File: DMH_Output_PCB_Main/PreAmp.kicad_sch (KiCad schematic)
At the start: 42 parts, among them J13 Conn_01x06, J28 Conn_01x06, J33 Conn_01x06, J35 Conn_01x04_PinHeader, J36 Conn_01x04_PinHeader, U16 NE5532, U17 NE5532, U18 NE5532, U19 NE5532

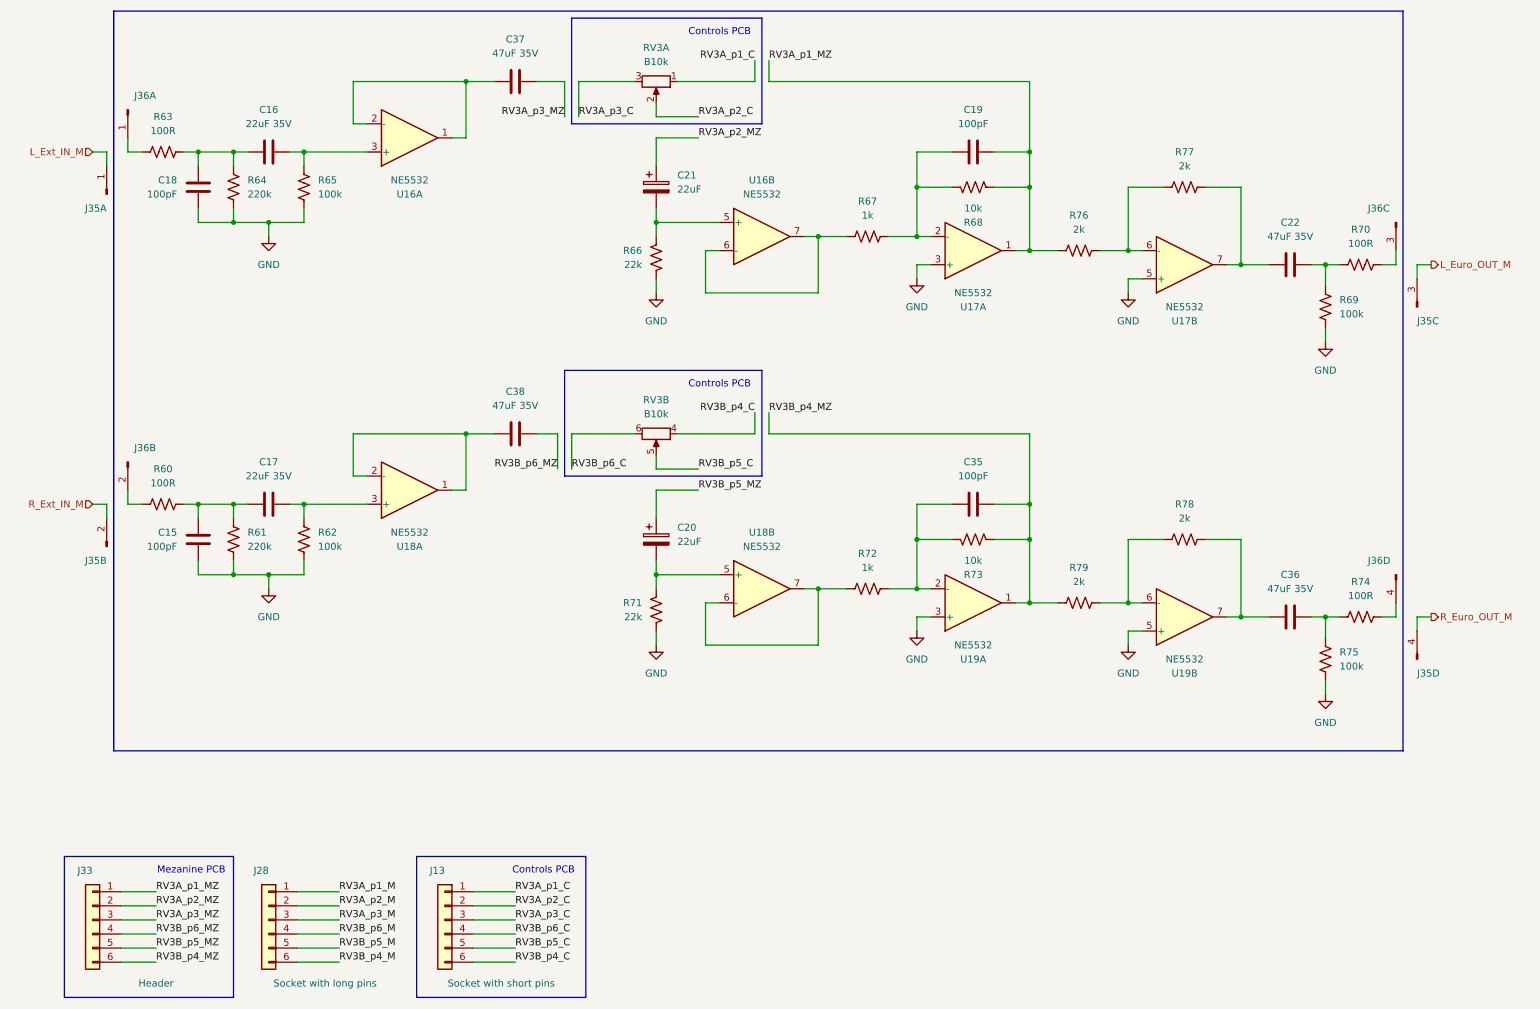
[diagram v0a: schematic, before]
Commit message: PCB Main comp placement done
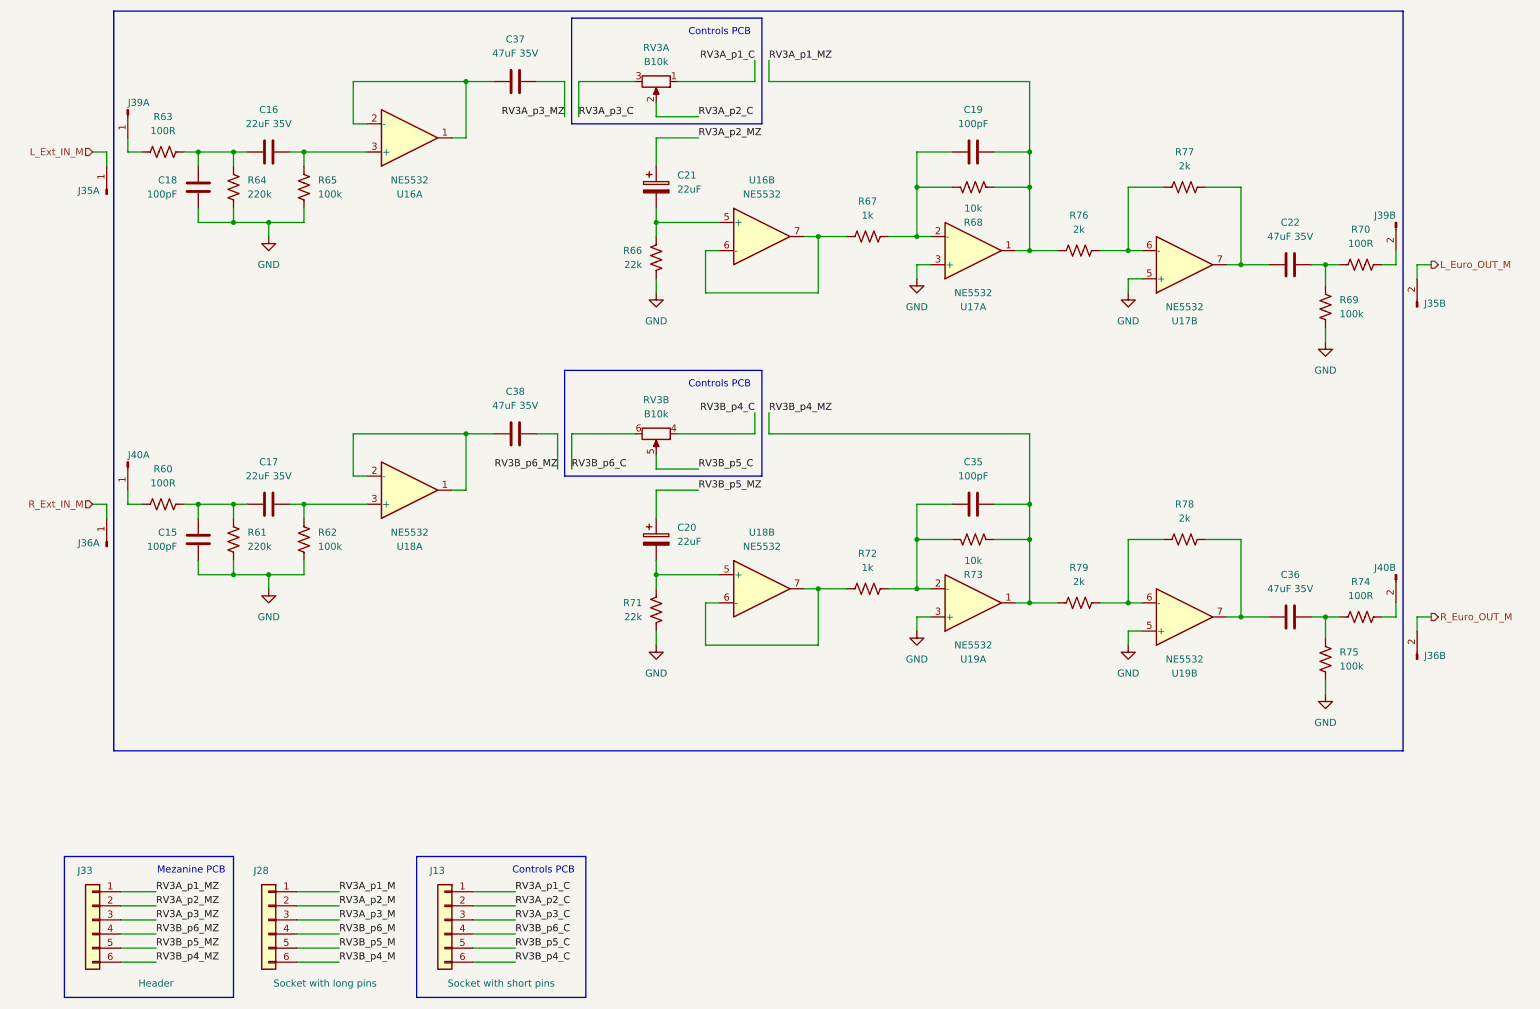
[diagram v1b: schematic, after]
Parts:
- removed J35: Conn_01x04_PinHeader, Connector_PinSocket_2.54mm:PinSocket_1x04_P2.54mm_Vertical, symbol SynthStuff:Conn_01x04_PinHeader
- removed J36: Conn_01x04_PinHeader, Connector_PinHeader_2.54mm:PinHeader_1x04_P2.54mm_Vertical, symbol SynthStuff:Conn_01x04_PinHeader
- added J35, J36: Conn_01x02_PinHeader, Connector_PinSocket_2.54mm:PinSocket_1x02_P2.54mm_Vertical, symbol SynthStuff:Conn_01x02_PinHeader
- added J39, J40: Conn_01x02_PinHeader, Connector_PinHeader_2.54mm:PinHeader_1x02_P2.54mm_Vertical, symbol SynthStuff:Conn_01x02_PinHeader
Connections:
- net L_Euro_OUT_M: now also J35.2 (Pin_2)
- net L_Ext_IN_M: now also J35.1 (Pin_1)
- net R_Euro_OUT_M: now also J36.2 (Pin_2)
- net R_Ext_IN_M: now also J36.1 (Pin_1)
- net at R74.2: now also J40.2 (Pin_2)
- net at R60.1: now also J40.1 (Pin_1)
- net at R70.2: now also J39.2 (Pin_2)
- net at R63.1: now also J39.1 (Pin_1)
